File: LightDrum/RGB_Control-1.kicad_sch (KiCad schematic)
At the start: 25 parts, among them U10 SQ2310ES_SOT23, U11 SQ2310ES_SOT23, U12 SQ2310ES_SOT23, U13 SQ2310ES_SOT23, U14 SQ2310ES_SOT23, U15 SQ2310ES_SOT23, U16 SQ2310ES_SOT23, U8 PCA9634_TSSOP20, U9 SQ2310ES_SOT23

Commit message: Add docs and gerbers for REV7
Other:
- title: RGB STRIP CONTROLLER 1 -> LightDrum
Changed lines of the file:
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@@
   (paper "A4")
   (title_block
-    (title "RGB STRIP CONTROLLER 1")
-    (rev "REV6")
+    (title "LightDrum")
+    (rev "REV7")
     (company "Daxxn Industries")
   )

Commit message: First pass over schematic (WIP)
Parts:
- R39, R41, R43, R45, R47, R49, R51, R53: value ${GATE-RES} -> 100
- R40, R42, R44, R46, R48, R50, R52, R54: value ${P-RES} -> 10K
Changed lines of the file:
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@@
   (title_block
     (title "LightDrum")
-    (rev "REV7")
+    (rev "REV8")
     (company "Daxxn Industries")
   )
@@
       (effects (font (size 1.27 1.27)) (justify right))
     )
-    (property "Value" "${GATE-RES}" (id 1) (at 107.95 73.406 0)
+    (property "Value" "100" (id 1) (at 107.95 73.406 0)
       (effects (font (size 1.27 1.27)) (justify right))
     )
@@
       (effects (font (size 1.27 1.27)) (justify right))
     )
-    (property "Value" "${GATE-RES}" (id 1) (at 184.15 73.406 0)
+    (property "Value" "100" (id 1) (at 184.15 73.406 0)
       (effects (font (size 1.27 1.27)) (justify right))
     )
@@
       (effects (font (size 1.27 1.27)) (justify right))
     )
-    (property "Value" "${P-RES}" (id 1) (at 171.45 56.896 0)
+    (property "Value" "10K" (id 1) (at 171.45 56.896 0)
       (effects (font (size 1.27 1.27)) (justify right))
     )
@@
       (effects (font (size 1.27 1.27)) (justify right))
     )
-    (property "Value" "${P-RES}" (id 1) (at 107.95 81.026 0)
+    (property "Value" "10K" (id 1) (at 107.95 81.026 0)
       (effects (font (size 1.27 1.27)) (justify right))
     )
@@
       (effects (font (size 1.27 1.27)) (justify right))
     )
-    (property "Value" "${GATE-RES}" (id 1) (at 171.45 49.276 0)
+    (property "Value" "100" (id 1) (at 171.45 49.276 0)
       (effects (font (size 1.27 1.27)) (justify right))
     )
@@
       (effects (font (size 1.27 1.27)) (justify right))
     )
-    (property "Value" "${P-RES}" (id 1) (at 120.65 56.896 0)
+    (property "Value" "10K" (id 1) (at 120.65 56.896 0)
       (effects (font (size 1.27 1.27)) (justify right))
     )
@@
       (effects (font (size 1.27 1.27)) (justify right))
     )
-    (property "Value" "${P-RES}" (id 1) (at 133.35 81.026 0)
+    (property "Value" "10K" (id 1) (at 133.35 81.026 0)
       (effects (font (size 1.27 1.27)) (justify right))
     )
@@
       (effects (font (size 1.27 1.27)) hide)
     )
-    (property "Datasheet" "C:\\Users\\Daxxn\\Documents\\Electrical\\Datasheets\\SQ2310ES.pdf" (id 3) (at 139.7 63.5 0)
+    (property "Datasheet" "%LOCAL_DATASHEETS%\\SQ2310ES.pdf" (id 3) (at 139.7 63.5 0)
       (effects (font (size 1.27 1.27)) hide)
     )
@@
       (effects (font (size 1.27 1.27)) hide)
     )
-    (property "Datasheet" "C:\\Users\\Daxxn\\Documents\\Electrical\\Datasheets\\SQ2310ES.pdf" (id 3) (at 152.4 39.37 0)
+    (property "Datasheet" "%LOCAL_DATASHEETS%\\SQ2310ES.pdf" (id 3) (at 152.4 39.37 0)
       (effects (font (size 1.27 1.27)) hide)
     )
@@
       (effects (font (size 1.27 1.27)) (justify right))
     )
-    (property "Value" "${P-RES}" (id 1) (at 158.75 81.026 0)
+    (property "Value" "10K" (id 1) (at 158.75 81.026 0)
       (effects (font (size 1.27 1.27)) (justify right))
     )
@@
       (effects (font (size 1.27 1.27)) (justify right))
     )
-    (property "Value" "${GATE-RES}" (id 1) (at 158.75 73.406 0)
+    (property "Value" "100" (id 1) (at 158.75 73.406 0)
       (effects (font (size 1.27 1.27)) (justify right))
     )
@@
       (effects (font (size 1.27 1.27)) hide)
     )
-    (property "Datasheet" "C:\\Users\\Daxxn\\Documents\\Electrical\\Datasheets\\SQ2310ES.pdf" (id 3) (at 190.5 63.5 0)
+    (property "Datasheet" "%LOCAL_DATASHEETS%\\SQ2310ES.pdf" (id 3) (at 190.5 63.5 0)
       (effects (font (size 1.27 1.27)) hide)
     )
@@
       (effects (font (size 1.27 1.27)) (justify right))
     )
-    (property "Value" "${GATE-RES}" (id 1) (at 120.65 49.276 0)
+    (property "Value" "100" (id 1) (at 120.65 49.276 0)
       (effects (font (size 1.27 1.27)) (justify right))
     )
@@
       (effects (font (size 1.27 1.27)) (justify right))
     )
-    (property "Value" "${GATE-RES}" (id 1) (at 95.25 49.276 0)
+    (property "Value" "100" (id 1) (at 95.25 49.276 0)
       (effects (font (size 1.27 1.27)) (justify right))
     )
@@
       (effects (font (size 1.27 1.27)) (justify right))
     )
-    (property "Value" "${P-RES}" (id 1) (at 95.25 56.896 0)
+    (property "Value" "10K" (id 1) (at 95.25 56.896 0)
       (effects (font (size 1.27 1.27)) (justify right))
     )
@@
       (effects (font (size 1.27 1.27)) (justify right))
     )
-    (property "Value" "${P-RES}" (id 1) (at 184.15 81.026 0)
+    (property "Value" "10K" (id 1) (at 184.15 81.026 0)
       (effects (font (size 1.27 1.27)) (justify right))
     )
@@
       (effects (font (size 1.27 1.27)) (justify right))
     )
-    (property "Value" "${P-RES}" (id 1) (at 146.05 56.896 0)
+    (property "Value" "10K" (id 1) (at 146.05 56.896 0)
       (effects (font (size 1.27 1.27)) (justify right))
     )
@@
       (effects (font (size 1.27 1.27)) hide)
     )
-    (property "Datasheet" "C:\\Users\\Daxxn\\Documents\\Electrical\\Datasheets\\PCA9634.pdf" (id 3) (at 45.72 16.51 0)
+    (property "Datasheet" "%LOCAL_DATASHEETS%\\PCA9634.pdf" (id 3) (at 45.72 16.51 0)
       (effects (font (size 1.27 1.27)) hide)
     )
@@
       (effects (font (size 1.27 1.27)) hide)
     )
-    (property "Datasheet" "C:\\Users\\Daxxn\\Documents\\Electrical\\Datasheets\\SQ2310ES.pdf" (id 3) (at 177.8 39.37 0)
+    (property "Datasheet" "%LOCAL_DATASHEETS%\\SQ2310ES.pdf" (id 3) (at 177.8 39.37 0)
       (effects (font (size 1.27 1.27)) hide)
     )
@@
       (effects (font (size 1.27 1.27)) hide)
     )
-    (property "Datasheet" "C:\\Users\\Daxxn\\Documents\\Electrical\\Datasheets\\SQ2310ES.pdf" (id 3) (at 114.3 63.5 0)
+    (property "Datasheet" "%LOCAL_DATASHEETS%\\SQ2310ES.pdf" (id 3) (at 114.3 63.5 0)
       (effects (font (size 1.27 1.27)) hide)
     )
@@
       (effects (font (size 1.27 1.27)) hide)
     )
-    (property "Datasheet" "C:\\Users\\Daxxn\\Documents\\Electrical\\Datasheets\\SQ2310ES.pdf" (id 3) (at 127 39.37 0)
+    (property "Datasheet" "%LOCAL_DATASHEETS%\\SQ2310ES.pdf" (id 3) (at 127 39.37 0)
       (effects (font (size 1.27 1.27)) hide)
     )
@@
       (effects (font (size 1.27 1.27)) hide)
     )
-    (property "Datasheet" "C:\\Users\\Daxxn\\Documents\\Electrical\\Datasheets\\SQ2310ES.pdf" (id 3) (at 165.1 63.5 0)
+    (property "Datasheet" "%LOCAL_DATASHEETS%\\SQ2310ES.pdf" (id 3) (at 165.1 63.5 0)
       (effects (font (size 1.27 1.27)) hide)
     )
@@
       (effects (font (size 1.27 1.27)) (justify right))
     )
-    (property "Value" "${GATE-RES}" (id 1) (at 133.35 73.406 0)
+    (property "Value" "100" (id 1) (at 133.35 73.406 0)
       (effects (font (size 1.27 1.27)) (justify right))
     )
@@
       (effects (font (size 1.27 1.27)) (justify right))
     )
-    (property "Value" "${GATE-RES}" (id 1) (at 146.05 49.276 0)
+    (property "Value" "100" (id 1) (at 146.05 49.276 0)
       (effects (font (size 1.27 1.27)) (justify right))
     )
@@
       (effects (font (size 1.27 1.27)) hide)
     )
-    (property "Datasheet" "C:\\Users\\Daxxn\\Documents\\Electrical\\Datasheets\\SQ2310ES.pdf" (id 3) (at 101.6 39.37 0)
-      (effects (font (size 1.27 1.27)) hide)
-    )
+    (property "Datasheet" "%LOCAL_DATASHEETS%\\SQ2310ES.pdf" (id 3) (at 101.6 39.37 0)
+      (effects (font (size 1.27 1.27)) hide)
+    )

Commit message: General component placement
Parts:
- U301: renamed from U8; PartNumber (none) -> 0806-0003
- U302: renamed from U9; PartNumber (none) -> 0703-0001
- U303: renamed from U11; PartNumber (none) -> 0703-0001
- U304: renamed from U13; PartNumber (none) -> 0703-0001
- U305: renamed from U15; PartNumber (none) -> 0703-0001
- U306: renamed from U10; PartNumber (none) -> 0703-0001
- U307: renamed from U12; PartNumber (none) -> 0703-0001
- U308: renamed from U14; PartNumber (none) -> 0703-0001
- U309: renamed from U16; PartNumber (none) -> 0703-0001
- renumbered R39 to R301, R43 to R302, R47 to R303, R51 to R304, R40 to R305, R44 to R306, R48 to R307, R52 to R308, R41 to R309, R45 to R310, R49 to R311, R53 to R312, R42 to R313, R46 to R314, R50 to R315, R54 to R316

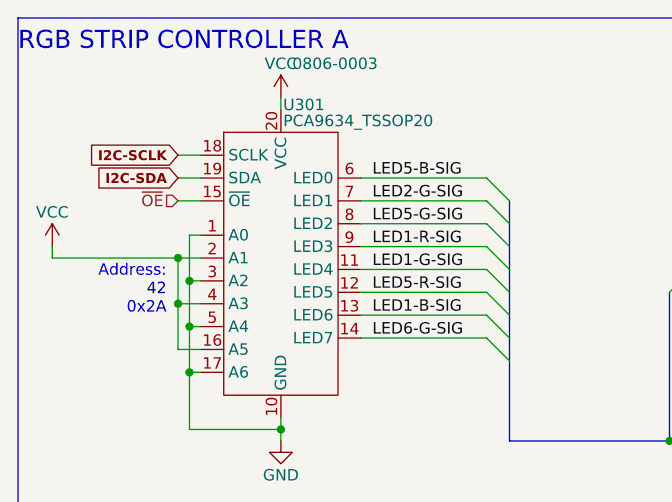
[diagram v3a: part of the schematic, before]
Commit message: Simplify analog power supply and add some routing
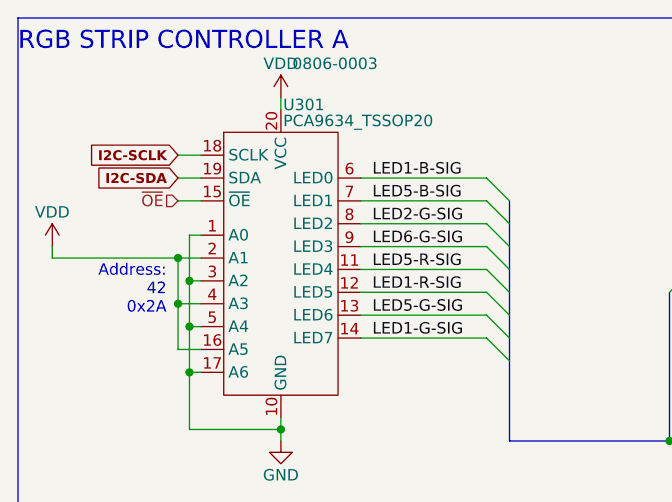
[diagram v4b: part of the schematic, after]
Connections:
- net LED1-B-SIG: now also U301.6 (LED0); no longer U301.13 (LED6)
- net LED1-G-SIG: now also U301.14 (LED7); no longer U301.11 (LED4)
- net LED1-R-SIG: now also U301.12 (LED5); no longer U301.9 (LED3)
- net LED2-G-SIG: now also U301.8 (LED2); no longer U301.7 (LED1)
- net LED5-B-SIG: now also U301.7 (LED1); no longer U301.6 (LED0)
- net LED5-G-SIG: now also U301.13 (LED6); no longer U301.8 (LED2)
- net LED5-R-SIG: now also U301.11 (LED4); no longer U301.12 (LED5)
- net LED6-G-SIG: now also U301.9 (LED3); no longer U301.14 (LED7)
- net VCC renamed VDD
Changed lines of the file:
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@@
     (effects (font (size 1.27 1.27)) (justify left bottom))
   )
-  (label "LED1-B-SIG" (at 55.88 49.53 0)
+  (label "LED1-B-SIG" (at 55.88 34.29 0)
     (effects (font (size 1.27 1.27)) (justify left bottom))
   )
@@
     (effects (font (size 1.27 1.27)) (justify left bottom))
   )
-  (label "LED5-R-SIG" (at 55.88 46.99 0)
+  (label "LED5-R-SIG" (at 55.88 44.45 0)
     (effects (font (size 1.27 1.27)) (justify left bottom))
   )
@@
     (effects (font (size 1.27 1.27)) (justify left bottom))
   )
-  (label "LED5-B-SIG" (at 55.88 34.29 0)
-    (effects (font (size 1.27 1.27)) (justify left bottom))
-  )
-  (label "LED2-G-SIG" (at 55.88 36.83 0)
-    (effects (font (size 1.27 1.27)) (justify left bottom))
-  )
-  (label "LED5-G-SIG" (at 55.88 39.37 0)
+  (label "LED5-B-SIG" (at 55.88 36.83 0)
+    (effects (font (size 1.27 1.27)) (justify left bottom))
+  )
+  (label "LED2-G-SIG" (at 55.88 39.37 0)
+    (effects (font (size 1.27 1.27)) (justify left bottom))
+  )
+  (label "LED5-G-SIG" (at 55.88 49.53 0)
     (effects (font (size 1.27 1.27)) (justify left bottom))
   )
@@
     (effects (font (size 1.27 1.27)) (justify left bottom))
   )
-  (label "LED1-R-SIG" (at 55.88 41.91 0)
-    (effects (font (size 1.27 1.27)) (justify left bottom))
-  )
-  (label "LED6-G-SIG" (at 55.88 52.07 0)
+  (label "LED1-R-SIG" (at 55.88 46.99 0)
+    (effects (font (size 1.27 1.27)) (justify left bottom))
+  )
+  (label "LED6-G-SIG" (at 55.88 41.91 0)
     (effects (font (size 1.27 1.27)) (justify left bottom))
   )
@@
     (effects (font (size 1.27 1.27)) (justify left bottom))
   )
-  (label "LED1-G-SIG" (at 55.88 44.45 0)
+  (label "LED1-G-SIG" (at 55.88 52.07 0)
     (effects (font (size 1.27 1.27)) (justify left bottom))
   )
@@
     (effects (font (size 1.27 1.27)) (justify left))
   )
+  (symbol (lib_id "power:VDD") (at 45.72 25.4 0) (unit 1)
+    (in_bom yes) (on_board yes)
+    (property "Reference" "#PWR0126" (id 0) (at 45.72 29.21 0)
+      (effects (font (size 1.27 1.27)) hide)
+    )
+    (property "Value" "VDD" (id 1) (at 45.72 21.59 0))
+    (property "Footprint" "" (id 2) (at 45.72 25.4 0)
+      (effects (font (size 1.27 1.27)) hide)
+    )
+    (property "Datasheet" "" (id 3) (at 45.72 25.4 0)
+      (effects (font (size 1.27 1.27)) hide)
+    )
+    (pin "1")
+  )
   (symbol (lib_id "Device:R_Small_US") (at 109.22 72.39 0) (unit 1)
     (in_bom yes) (on_board yes)
@@
     (pin "2")
     (pin "3")
-  )
-  (symbol (lib_id "power:VCC") (at 45.72 25.4 0) (unit 1)
-    (in_bom yes) (on_board yes)
-    (property "Reference" "#PWR0301" (id 0) (at 45.72 29.21 0)
-      (effects (font (size 1.27 1.27)) hide)
-    )
-    (property "Value" "VCC" (id 1) (at 45.72 21.59 0))
-    (property "Footprint" "" (id 2) (at 45.72 25.4 0)
-      (effects (font (size 1.27 1.27)) hide)
-    )
-    (property "Datasheet" "" (id 3) (at 45.72 25.4 0)
-      (effects (font (size 1.27 1.27)) hide)
-    )
-    (pin "1")
   )
   (symbol (lib_id "Device:R_Small_US") (at 121.92 48.26 0) (unit 1)
@@
     (pin "3")
   )
-  (symbol (lib_id "power:VCC") (at 20.32 41.91 0) (unit 1)
-    (in_bom yes) (on_board yes)
-    (property "Reference" "#PWR0302" (id 0) (at 20.32 45.72 0)
-      (effects (font (size 1.27 1.27)) hide)
-    )
-    (property "Value" "VCC" (id 1) (at 20.32 38.1 0))
+  (symbol (lib_id "Daxxn_Transistors:SQ2310ES_SOT23") (at 113.03 76.2 0) (unit 1)
+    (in_bom yes) (on_board yes)
+    (property "Reference" "U306" (id 0) (at 115.57 74.93 0)
+      (effects (font (size 1.27 1.27)) (justify left))
+    )
+    (property "Value" "SQ2310ES_SOT23" (id 1) (at 115.57 77.47 0)
+      (effects (font (size 0.85 0.85)) (justify left))
+    )
+    (property "Footprint" "Package_TO_SOT_SMD:SOT-23" (id 2) (at 114.3 60.96 0)
+      (effects (font (size 1.27 1.27)) hide)
+    )
+    (property "Datasheet" "%LOCAL_DATASHEETS%\\SQ2310ES.pdf" (id 3) (at 114.3 63.5 0)
+      (effects (font (size 1.27 1.27)) hide)
+    )
+    (property "PartNumber" "0703-0001" (id 4) (at 115.57 72.39 0)
+      (effects (font (size 1.27 1.27)) (justify left))
+    )
+    (pin "1")
+    (pin "2")
+    (pin "3")
+  )
+  (symbol (lib_name "SQ2310ES_SOT23_4") (lib_id "Daxxn_Transistors:SQ2310ES_SOT23") (at 125.73 52.07 0) (unit 1)
+    (in_bom yes) (on_board yes)
+    (property "Reference" "U303" (id 0) (at 128.27 50.8 0)
+      (effects (font (size 1.27 1.27)) (justify left))
+    )
+    (property "Value" "SQ2310ES_SOT23" (id 1) (at 128.27 53.34 0)
+      (effects (font (size 0.85 0.85)) (justify left))
+    )
+    (property "Footprint" "Package_TO_SOT_SMD:SOT-23" (id 2) (at 127 36.83 0)
+      (effects (font (size 1.27 1.27)) hide)
+    )
+    (property "Datasheet" "%LOCAL_DATASHEETS%\\SQ2310ES.pdf" (id 3) (at 127 39.37 0)
+      (effects (font (size 1.27 1.27)) hide)
+    )
+    (property "PartNumber" "0703-0001" (id 4) (at 128.27 48.26 0)
+      (effects (font (size 1.27 1.27)) (justify left))
+    )
+    (pin "1")
+    (pin "2")
+    (pin "3")
+  )
+  (symbol (lib_name "SQ2310ES_SOT23_6") (lib_id "Daxxn_Transistors:SQ2310ES_SOT23") (at 163.83 76.2 0) (unit 1)
+    (in_bom yes) (on_board yes)
+    (property "Reference" "U308" (id 0) (at 166.37 74.93 0)
+      (effects (font (size 1.27 1.27)) (justify left))
+    )
+    (property "Value" "SQ2310ES_SOT23" (id 1) (at 166.37 77.47 0)
+      (effects (font (size 0.85 0.85)) (justify left))
+    )
+    (property "Footprint" "Package_TO_SOT_SMD:SOT-23" (id 2) (at 165.1 60.96 0)
+      (effects (font (size 1.27 1.27)) hide)
+    )
+    (property "Datasheet" "%LOCAL_DATASHEETS%\\SQ2310ES.pdf" (id 3) (at 165.1 63.5 0)
+      (effects (font (size 1.27 1.27)) hide)
+    )
+    (property "PartNumber" "0703-0001" (id 4) (at 166.37 72.39 0)
+      (effects (font (size 1.27 1.27)) (justify left))
+    )
+    (pin "1")
+    (pin "2")
+    (pin "3")
+  )
+  (symbol (lib_id "power:VDD") (at 20.32 41.91 0) (unit 1)
+    (in_bom yes) (on_board yes)
+    (property "Reference" "#PWR0125" (id 0) (at 20.32 45.72 0)
+      (effects (font (size 1.27 1.27)) hide)
+    )
+    (property "Value" "VDD" (id 1) (at 20.32 38.1 0))
     (property "Footprint" "" (id 2) (at 20.32 41.91 0)
       (effects (font (size 1.27 1.27)) hide)
@@
     (pin "1")
   )
-  (symbol (lib_id "Daxxn_Transistors:SQ2310ES_SOT23") (at 113.03 76.2 0) (unit 1)
-    (in_bom yes) (on_board yes)
-    (property "Reference" "U306" (id 0) (at 115.57 74.93 0)
-      (effects (font (size 1.27 1.27)) (justify left))
-    )
-    (property "Value" "SQ2310ES_SOT23" (id 1) (at 115.57 77.47 0)
-      (effects (font (size 0.85 0.85)) (justify left))
-    )
-    (property "Footprint" "Package_TO_SOT_SMD:SOT-23" (id 2) (at 114.3 60.96 0)
-      (effects (font (size 1.27 1.27)) hide)
-    )
-    (property "Datasheet" "%LOCAL_DATASHEETS%\\SQ2310ES.pdf" (id 3) (at 114.3 63.5 0)
-      (effects (font (size 1.27 1.27)) hide)
-    )
-    (property "PartNumber" "0703-0001" (id 4) (at 115.57 72.39 0)
-      (effects (font (size 1.27 1.27)) (justify left))
-    )
-    (pin "1")
-    (pin "2")
-    (pin "3")
-  )
-  (symbol (lib_name "SQ2310ES_SOT23_4") (lib_id "Daxxn_Transistors:SQ2310ES_SOT23") (at 125.73 52.07 0) (unit 1)
-    (in_bom yes) (on_board yes)
-    (property "Reference" "U303" (id 0) (at 128.27 50.8 0)
-      (effects (font (size 1.27 1.27)) (justify left))
-    )
-    (property "Value" "SQ2310ES_SOT23" (id 1) (at 128.27 53.34 0)
-      (effects (font (size 0.85 0.85)) (justify left))
-    )
-    (property "Footprint" "Package_TO_SOT_SMD:SOT-23" (id 2) (at 127 36.83 0)
-      (effects (font (size 1.27 1.27)) hide)
-    )
-    (property "Datasheet" "%LOCAL_DATASHEETS%\\SQ2310ES.pdf" (id 3) (at 127 39.37 0)
-      (effects (font (size 1.27 1.27)) hide)
-    )
-    (property "PartNumber" "0703-0001" (id 4) (at 128.27 48.26 0)
-      (effects (font (size 1.27 1.27)) (justify left))
-    )
-    (pin "1")
-    (pin "2")
-    (pin "3")
-  )
-  (symbol (lib_name "SQ2310ES_SOT23_6") (lib_id "Daxxn_Transistors:SQ2310ES_SOT23") (at 163.83 76.2 0) (unit 1)
-    (in_bom yes) (on_board yes)
-    (property "Reference" "U308" (id 0) (at 166.37 74.93 0)
-      (effects (font (size 1.27 1.27)) (justify left))
-    )
-    (property "Value" "SQ2310ES_SOT23" (id 1) (at 166.37 77.47 0)
-      (effects (font (size 0.85 0.85)) (justify left))
-    )
-    (property "Footprint" "Package_TO_SOT_SMD:SOT-23" (id 2) (at 165.1 60.96 0)
-      (effects (font (size 1.27 1.27)) hide)
-    )
-    (property "Datasheet" "%LOCAL_DATASHEETS%\\SQ2310ES.pdf" (id 3) (at 165.1 63.5 0)
-      (effects (font (size 1.27 1.27)) hide)
-    )
-    (property "PartNumber" "0703-0001" (id 4) (at 166.37 72.39 0)
-      (effects (font (size 1.27 1.27)) (justify left))
-    )
-    (pin "1")
-    (pin "2")
-    (pin "3")
-  )
   (symbol (lib_id "Device:R_Small_US") (at 134.62 72.39 0) (unit 1)
